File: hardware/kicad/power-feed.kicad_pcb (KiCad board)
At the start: 4 copper layers, 100 x 100 mm, 159 parts, among them J1 36V IN, J2 MOTOR A+ A- B+ B-, J3 CLUTCH COIL, J4 PANEL 2x7 IDC, J5 JST-XH 7p, Q1 SQD50P06-15L, Q10 CSD88537ND, Q11 CSD88537ND, Q12 CSD88537ND, Q13 CSD88537ND, Q2 AGM60P20R, Q3 2N7002, Q4 SI2308A, SW1 RESET, U1 LM5164DDAR, U2 TMC5160A-TA, U3 74LVC1G00, U4 74AHCT1G08, U5 74AHCT1G08, U6 TLV9061

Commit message: Finish controller PCB: DRC clean, silkscreen, JLCPCB fab outputs
- manual_fixes.py closes the last 5 DRC errors: In2 +3V3 corridor extended
  under U2 VCC_IO vias, B.Cu +3V3 feed for the clutch op-amp, C19 bootstrap
  cap flipped with CA1/HA1/MOT_A1 re-routed, GND vias at the D9/D10 ESD
  arrays' isolated pads; redundant via-in-pad vias removed. DRC: 0 errors,
  0 unconnected, parity clean.
- silk_cleanup.py: passive references to F.Fab, remaining references
  relocated clear of pads/silk/edge, connector pin labels, 36V MAX warning
  and board title (silk warnings 153 -> 0).
- export_fab.py: Gerbers, Excellon drills + maps, JLC BOM/CPL, zip and
  hardware/fab/README.md with board specs and parts lacking LCSC numbers.
- New 3D renders.

Co-Authored-By: Claude Fable 5.1 <noreply@anthropic.com>
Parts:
- turned C19 to 180 degrees
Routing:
- net +3V3: track 81.6 -> 101.5 mm, vias 18 -> 22
- net /TMC5160 stepper driver/TMC_CA1: track 1.09 -> 4.41 mm, vias 1 -> 0
- net GND: track 219.0 -> 220.6 mm, vias 523 -> 525
- net /TMC5160 stepper driver/TMC_HA1: track 7.47 -> 6.33 mm
- net /TMC5160 stepper driver/MOT_A1: track 51.6 -> 50.9 mm
- net /TMC5160 stepper driver/TMC_LB2: vias 3 -> 2
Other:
- board text added: "36V MAX"
- board text added: "36V+"
- board text added: "A+"
- board text added: "A-"
- board text added: "B+"
- board text added: "B-"
- board text added: "COIL+"
- board text added: "COIL-"
- board text added: "GND"
- board text added: "MILL POWER FEED v1"

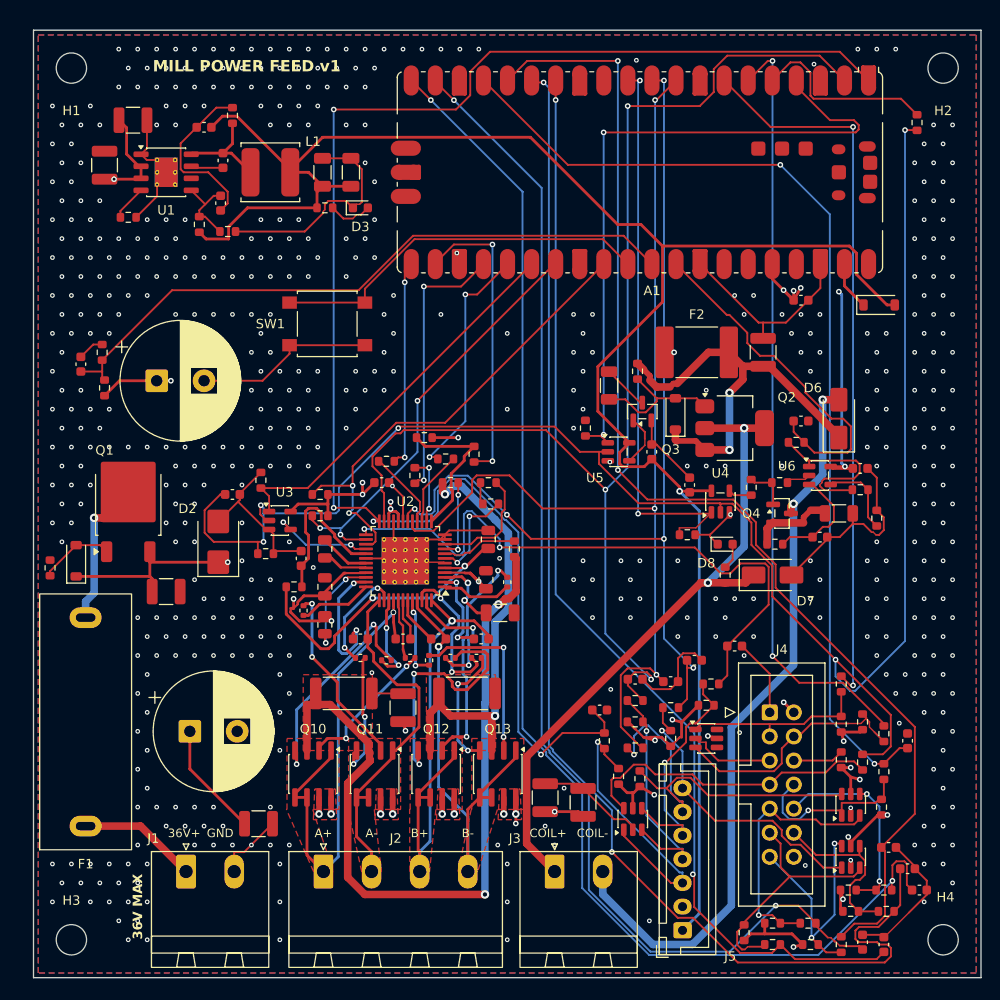
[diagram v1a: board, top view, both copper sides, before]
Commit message: PCB: finish layout review fixes 1-9, replace the Pico module with the bare RP2040 circuit
Part A (hardware/tools/layout_fixes_v2.py, rerunnable):
- review fixes 1-9 finished; new fix10 drops GND stitching vias that end up
  too close to the reroutes
- 36 V nets keep 0.5 mm on the outer layers (power-feed.kicad_dru), with
  documented exceptions inside the TMC/FET packages
- the 1210 bridge caps under Q10-Q13 and the USB-C / J6 / H4 corner have
  explicit courtyard-overlap rules

Part B (hardware/tools/rp2040_layout.py, runs after layout_fixes_v2.py):
- Footprints are synced from the schematic (refs renumbered via refmap.py)
  and A1 is removed.
- U3 RP2040 sits at (60, 13), with flash U4, crystal Y1 (no vias in the
  crystal loop), decoupling, EP vias into In1, and the AP2112K (U5) feeding
  +3V3.
- USB-C J4 is on the bottom edge at (87.6, 96.35), with the D+/D- pair and
  the 27R resistors at the MCU.
- SW1 BOOTSEL, SW2 RESET and J3 SWD are on top.
- All copper of the RP2040 nets is replayed from rp2040_routes.json (Freerouting
  plus hand routes). LIM_L / ENC_OUT_B leave the QFN through vias inside the
  pad ring and run on B.Cu.
- No-connect pad nets use KiCad's {slash} escaping, so schematic parity is
  clean.

check_pcb.py: PASS. 0 errors, 0 unconnected, 0 parity issues. There are 11
silk warnings: 7 from Part A (motor labels, J2 outline, B- label) and 4 from
the J4 outline at the edge and over its shield peg.
Fab outputs are regenerated. The BOM/CPL include U3/U4/U5/Y1/J4, and J3 is a
hand-soldered THT header.

Co-Authored-By: Claude Opus 5.5 <noreply@anthropic.com>
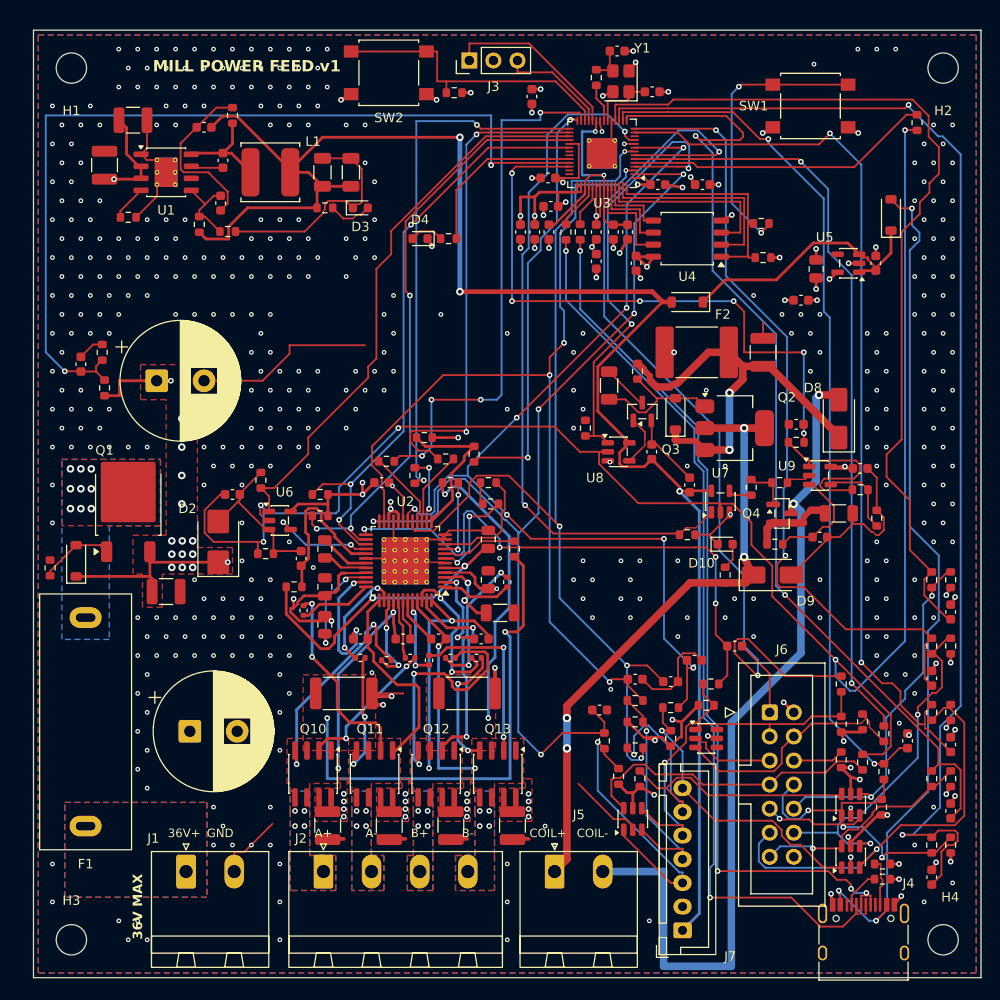
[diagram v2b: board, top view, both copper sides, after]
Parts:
- removed A1: Raspberry Pi Pico, Module:RaspberryPi_Pico_SMD
- added C29: 100nF, Capacitor_SMD:C_0603_1608Metric, F.Cu at (65.9, 16.3)
- added C30: 100nF, Capacitor_SMD:C_0603_1608Metric, F.Cu at (70.6, 16.3)
- added C31: 100nF, Capacitor_SMD:C_0603_1608Metric, F.Cu at (52.6, 7.00)
- added C32: 100nF, Capacitor_SMD:C_0603_1608Metric, F.Cu at (54.6, 18.6)
- added C33: 100nF, Capacitor_SMD:C_0603_1608Metric, F.Cu at (54.3, 15.6)
- added C35: 100nF, Capacitor_SMD:C_0603_1608Metric, F.Cu at (59.4, 24.4)
- added C36: 1uF, Capacitor_SMD:C_0603_1608Metric, F.Cu at (52.9, 21.3)
- added C37: 1uF, Capacitor_SMD:C_0603_1608Metric, F.Cu at (54.4, 21.3)
- added C38: 100nF, Capacitor_SMD:C_0603_1608Metric, F.Cu at (61.2, 21.3)
- added C39: 100nF, Capacitor_SMD:C_0603_1608Metric, F.Cu at (62.7, 21.3)
- added C40: 100nF, Capacitor_SMD:C_0603_1608Metric, F.Cu at (51.4, 21.3)
- added C41: 15pF, Capacitor_SMD:C_0603_1608Metric, F.Cu at (65.3, 6.50)
- added C42: 15pF, Capacitor_SMD:C_0603_1608Metric, F.Cu at (61.6, 2.20)
- added C43: 1uF, Capacitor_SMD:C_0603_1608Metric, F.Cu at (88.9, 24.6)
- added C44: 4.7uF 10V, Capacitor_SMD:C_0805_2012Metric, F.Cu at (82.6, 25.2)
- added C45: 100nF, Capacitor_SMD:C_0603_1608Metric, F.Cu at (59.4, 21.3)
- added C51: 100nF, Capacitor_SMD:C_0603_1608Metric, F.Cu at (63.6, 24.6)
- added D4: green, LED_SMD:LED_0603_1608Metric, F.Cu at (40.8, 22.0)
- added D6: B5819W, Diode_SMD:D_SOD-123, F.Cu at (90.5, 19.5)
- added J3: SWD, Connector_PinHeader_2.54mm:PinHeader_1x03_P2.54mm_Vertical, F.Cu at (46.0, 3.20)
- added J4: USB-C, Connector_USB:USB_C_Receptacle_HRO_TYPE-C-31-M-12, F.Cu at (87.6, 96.3)
- added R24: 10k, Resistor_SMD:R_0603_1608Metric, F.Cu at (77.0, 24.0)
- added R25: 1k, Resistor_SMD:R_0603_1608Metric, F.Cu at (76.8, 20.4)
- added R26: 1k, Resistor_SMD:R_0603_1608Metric, F.Cu at (59.4, 5.00)
- added R27: 10k, Resistor_SMD:R_0603_1608Metric, F.Cu at (44.4, 6.60)
- added R28: 1k, Resistor_SMD:R_0603_1608Metric, F.Cu at (43.8, 22.0)
- added R29: 5.1k, Resistor_SMD:R_0603_1608Metric, F.Cu at (89.6, 89.6)
- added R30: 5.1k, Resistor_SMD:R_0603_1608Metric, F.Cu at (89.6, 88.0)
- added R31: 27, Resistor_SMD:R_0603_1608Metric, F.Cu at (57.7, 21.3)
- added R32: 27, Resistor_SMD:R_0603_1608Metric, F.Cu at (56.2, 21.3)
- added SW1: BOOTSEL, Button_Switch_SMD:SW_SPST_B3S-1000, F.Cu at (82.0, 8.00)
- added U3: RP2040, Package_DFN_QFN:QFN-56-1EP_7x7mm_P0.4mm_EP3.2x3.2mm_ThermalVias, F.Cu at (60.0, 13.0)
- added U4: W25Q128JVS, Package_SO:SOIC-8_5.3x5.3mm_P1.27mm, F.Cu at (69.0, 22.0)
- added U5: AP2112K-3.3, Package_TO_SOT_SMD:SOT-23-5, F.Cu at (86.0, 24.6)
- added Y1: 12MHz, Crystal:Crystal_SMD_3225-4Pin_3.2x2.5mm, F.Cu at (62.0, 5.40)
- moved R61 34.5 mm to (96.8, 58.0), turned to 90 degrees
- moved R62 33.1 mm to (94.8, 58.0), turned to 90 degrees
- moved R67 31.9 mm to (96.8, 72.0)
- moved R69 29.9 mm to (96.8, 65.0), turned to 90 degrees
- moved R68 29.7 mm to (94.8, 72.0), turned to 90 degrees
- moved C55 29.5 mm to (96.8, 61.4), turned to 90 degrees
- moved R70 28.4 mm to (94.8, 65.0), turned to 90 degrees
- moved SW2 27.3 mm to (37.5, 4.50)
- moved R71 22.9 mm to (96.8, 79.0), turned to 90 degrees
- moved C58 22.2 mm to (96.8, 75.4)
- moved R59 20.5 mm to (96.8, 86.0), turned to 90 degrees
- moved C59 20.3 mm to (94.8, 68.4), turned to 90 degrees
- moved D5 20.3 mm to (69.0, 28.7), turned to 180 degrees
- moved R72 19.9 mm to (94.8, 79.0)
- moved R60 15.4 mm to (94.8, 86.0), turned to 90 degrees
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- renumbered C29 to C46, C30 to C47, C31 to C48, C32 to C49, C33 to C50, C35 to C52, C36 to C53, C37 to C54, C38 to C55, C39 to C56, C40 to C57, C41 to C58, C42 to C59, C43 to C60, C44 to C61, C45 to C62, C46 to C63, D8 to D10, D9 to D11, D10 to D12, D11 to D13, D12 to D14, D4 to D5, D5 to D7, D6 to D8, D7 to D9, J3 to J5, J4 to J6, J5 to J7, R24 to R33, R25 to R34, R26 to R35, R27 to R36, R28 to R37, R29 to R38, R30 to R39, R31 to R40, R32 to R41, R33 to R42, R34 to R43, R35 to R44, R36 to R45, R37 to R46, R38 to R47, R39 to R48, R40 to R49, R41 to R50, R42 to R51, R43 to R52, R44 to R53, R45 to R54, R46 to R55, R47 to R56, R48 to R57, R49 to R58, R50 to R59, R51 to R60, R52 to R61, R53 to R62, R54 to R63, R55 to R64, R56 to R65, R57 to R66, R58 to R67, R59 to R68, R60 to R69, R61 to R70, R62 to R71, R63 to R72, R64 to R73, R65 to R74, R66 to R75, R67 to R76, R68 to R77, R69 to R78, R70 to R79, R71 to R80, R72 to R81, R73 to R82, SW1 to SW2, U3 to U6, U4 to U7, U5 to U8, U6 to U9
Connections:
- net /Pico, SPI, E-stop interlock/CLUTCH_HS_PWM renamed /RP2040, SPI, E-stop interlock/CLUTCH_HS_PWM
- net /Pico, SPI, E-stop interlock/CLUTCH_LS_EN renamed /RP2040, SPI, E-stop interlock/CLUTCH_LS_EN
- net /Pico, SPI, E-stop interlock/DRV_EN renamed /RP2040, SPI, E-stop interlock/DRV_EN
- net /Pico, SPI, E-stop interlock/E_OK renamed /RP2040, SPI, E-stop interlock/E_OK
- D5 pad 1: /Pico, SPI, E-stop interlock/VSYS -> /RP2040, SPI, E-stop interlock/VSYS
- R33 pad 1: /Pico, SPI, E-stop interlock/SPI_SCK -> /RP2040, SPI, E-stop interlock/SPI_SCK
- R34 pad 1: /Pico, SPI, E-stop interlock/SPI_MOSI -> /RP2040, SPI, E-stop interlock/SPI_MOSI
- R35 pad 1: /Pico, SPI, E-stop interlock/SPI_CS -> /RP2040, SPI, E-stop interlock/SPI_CS
- R36 pad 2: /Pico, SPI, E-stop interlock/SPI_MISO -> /RP2040, SPI, E-stop interlock/SPI_MISO
- R46 pad 2: /Pico, SPI, E-stop interlock/E_OK_SENSE -> /RP2040, SPI, E-stop interlock/E_OK_SENSE
- SW2 pad 1: /Pico, SPI, E-stop interlock/RUN -> /RP2040, SPI, E-stop interlock/RUN
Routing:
- net /RP2040, SPI, E-stop interlock/USB_CONN_DM: track 0.00 -> 96.3 mm, vias 0 -> 2
- net /RP2040, SPI, E-stop interlock/USB_CONN_DP: track 0.00 -> 92.8 mm, vias 0 -> 4
- net /RP2040, SPI, E-stop interlock/VBUS: track 0.00 -> 91.5 mm, vias 0 -> 3
- net ENC_OUT_A: track 165.6 -> 106.8 mm, vias 4 -> 5
- net /RP2040, SPI, E-stop interlock/SPI_MISO: track 0.00 -> 56.1 mm, vias 0 -> 4
- net /RP2040, SPI, E-stop interlock/SPI_SCK: track 0.00 -> 56.0 mm, vias 0 -> 2
- net /RP2040, SPI, E-stop interlock/SPI_MOSI: track 0.00 -> 52.4 mm, vias 0 -> 2
- net DIAL_B: track 135.7 -> 84.6 mm
- net /RP2040, SPI, E-stop interlock/SPI_CS: track 0.00 -> 44.2 mm, vias 0 -> 2
- net RAPID: track 139.1 -> 95.2 mm, vias 2 -> 0
- net /Pico, SPI, E-stop interlock/RUN: track 40.4 -> 0.00 mm
- net ENC_OUT_B: track 133.0 -> 99.1 mm, vias 3 -> 4
- net /RP2040, SPI, E-stop interlock/E_OK_SENSE: track 0.00 -> 32.3 mm
- net /Pico, SPI, E-stop interlock/SPI_CS: track 31.8 -> 0.00 mm, vias 2 -> 0
- net /RP2040, SPI, E-stop interlock/RUN: track 0.00 -> 31.4 mm
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- added copper zone on B.Cu, net /Power input, protection, 5 V buck/VIN_F
- added copper zone on F.Cu, net /Power input, protection, 5 V buck/VIN_F
- added copper zone on B.Cu, net /Power input, protection, 5 V buck/VIN_RAW
- added copper zone on F.Cu, net /Power input, protection, 5 V buck/VIN_RAW
- added copper zone on B.Cu, net /TMC5160 stepper driver/MOT_A1
- added copper zone on B.Cu, net /TMC5160 stepper driver/MOT_A2
- added copper zone on B.Cu, net /TMC5160 stepper driver/MOT_B1
- added copper zone on B.Cu, net /TMC5160 stepper driver/MOT_B2

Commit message: PCB review round 2: bridge-cap and sense-resistor GND vias, USB off the +36V split, ESD + VDD_CORE cap
- C20/C22/C24/C26: the GND vias that fix2 added were removed again by its own
  stitching-via clean-up. They are now added after the clean-up, with tracks ending
  on their centres: 3 vias at C20/C26 and 2 at C22/C24, where the next J2 pad is
  close.
- R18/R21 pad 2: solid GND islands with 6 / 7 vias (0.6/0.3) into In1.
- USB pair and I2C_SCL now run east on B.Cu above the In2 +36V finger. The
  finger is cut to y 33.5-53, which also clears LIM_R's drop. No B.Cu signal
  crosses the split now.
- Schematic round 2 (04bb841) pulled in. refmap.OLD2NEW2 renumbers C40..C63
  -> C41..C64 and U5..U9 -> U6..U10.
  - New C40 (VDD_CORE 100 nF) at U3 pin 23 (59.2, 6.0). R26 moves to (58.5, 2.55)
    and XOUT is rerouted beside the crystal. Y1's GND pads are tied through
    the middle of the crystal.
  - New U5 USBLC6-2SC6 (79.5, 95.6), flow-through on the pair, just west of J4.
- U3 exposed pad: 5 more 0.6/0.3 vias.
- Docs: 1 oz outer copper, not 2 oz.
- The docstrings now state what was not done: the SRAL/SRBL Kelvin returns
  (no corridor found) and the SNS_A neck (0.85 mm at one pinch).

check_pcb: PASS (0 errors, 0 unconnected, 0 parity); 11 silk warnings as before.
Replays reproduce the board exactly: from f8aeb1d (pre-RP2040) and from 3838879.

Co-Authored-By: Claude Opus 5.5 <noreply@anthropic.com>
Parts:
- added C40: 100nF, Capacitor_SMD:C_0603_1608Metric, F.Cu at (59.2, 6.00)
- added U5: USBLC6-2SC6, Package_TO_SOT_SMD:SOT-23-6, F.Cu at (79.5, 95.6)
- moved R26 2.61 mm to (58.5, 2.55), turned to 0 degrees
- renumbered C40 to C41, C41 to C42, C42 to C43, C43 to C44, C44 to C45, C45 to C46, C46 to C47, C47 to C48, C48 to C49, C49 to C50, C50 to C51, C51 to C52, C52 to C53, C53 to C54, C54 to C55, C55 to C56, C56 to C57, C57 to C58, C58 to C59, C59 to C60, C60 to C61, C61 to C62, C62 to C63, C63 to C64, U9 to U10, U5 to U6, U6 to U7, U7 to U8, U8 to U9
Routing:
- net GND: track 229.2 -> 247.7 mm, vias 449 -> 473
- net /RP2040, SPI, E-stop interlock/USB_CONN_DP: track 92.8 -> 105.8 mm
- net /RP2040, SPI, E-stop interlock/USB_CONN_DM: track 96.3 -> 105.9 mm
- net /RP2040, SPI, E-stop interlock/VBUS: track 91.5 -> 101.0 mm, vias 3 -> 4
- net I2C_SCL: track 99.4 -> 106.5 mm
- net /RP2040, SPI, E-stop interlock/XOUT: track 4.07 -> 9.42 mm
- net /RP2040, SPI, E-stop interlock/VDD_CORE: track 25.7 -> 28.4 mm

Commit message: PCB review round 3: no vias inside the RP2040 exposed-pad paste windows
The four 0.6/0.3 vias at (59.25/60.75, 12.25/13.75) sat in the EP's paste windows, open under the paste,
and could wick the solder away from the RP2040's only GND joint. Removed from the board, from the pre-route list in
rp2040_layout.py and from rp2040_routes.json (replay reproduces the board: 733 vias, 1730 tracks). EP keeps the
footprint's 4 corner vias + 1 in the gap between the windows. DRC + parity PASS; fab outputs and renders regenerated.

Co-Authored-By: Claude Opus 5.5 <noreply@anthropic.com>
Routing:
- net GND: vias 473 -> 469
